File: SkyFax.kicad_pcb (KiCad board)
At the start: 2 copper layers, 60 parts, among them J1 RJ11/12, J2 DE9_Receptacle_MountingHoles, Q1 Q_NPN_BEC, Q2 Q_PNP_BEC, Q3 Q_NPN_BEC, Q4 Q_NPN_BEC, Q5 Q_NPN_BEC, Q6 Q_NPN_EBC, SW1 SW_DIP_x08, U1 Si2494-A-FM, U2 Si3018, U3 25LC640AT-E/SN, X1 ECS-2520MV-xxx-xx

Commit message: Sent to fab v1.0
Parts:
- removed kibuzzard-649E5FCF: G***, kibuzzard-649E5FCF
- removed kibuzzard-649E606C: G***, kibuzzard-649E606C
- removed kibuzzard-649E607D: G***, kibuzzard-649E607D
- removed kibuzzard-649E6159: G***, kibuzzard-649E6159
- added BZ1: Buzzer, Buzzer_Beeper:Buzzer_12x9.5RM7.6, F.Cu at (108.2, 146.6)
- added G***: LOGO, FaxCam:smiley_5.0x5.2mm, F.Cu at (151.1, 121.6)
- added J3: Conn_01x02, Connector_PinHeader_2.54mm:PinHeader_1x02_P2.54mm_Vertical, F.Cu at (95.8, 148.0)
- added kibuzzard-64A46BC3: G***, kibuzzard-64A46BC3, F.Cu at (161.6, 118.1)
- added kibuzzard-64A46BC7: G***, kibuzzard-64A46BC7, F.Cu at (152.9, 117.1)
- added kibuzzard-64A46BF2: G***, kibuzzard-64A46BF2, F.Cu at (156.7, 119.5)
- added kibuzzard-64A46C0A: G***, kibuzzard-64A46C0A, F.Cu at (160.1, 122.0)
- added kibuzzard-64A46CB2: G***, kibuzzard-64A46CB2, F.Cu at (97.0, 124.7)
- added kibuzzard-64A46CE2: G***, kibuzzard-64A46CE2, F.Cu at (99.6, 124.7)
- added kibuzzard-64A46CEC: G***, kibuzzard-64A46CEC, F.Cu at (102.1, 124.7)
- added kibuzzard-64A46CF4: G***, kibuzzard-64A46CF4, F.Cu at (104.6, 124.7)
- added kibuzzard-64A46CF9: G***, kibuzzard-64A46CF9, F.Cu at (107.2, 124.7)
- added kibuzzard-64A46D01: G***, kibuzzard-64A46D01, F.Cu at (109.7, 124.7)
- added kibuzzard-64A46D0F: G***, kibuzzard-64A46D0F, F.Cu at (112.3, 124.7)
- added kibuzzard-64A46D1C: G***, kibuzzard-64A46D1C, F.Cu at (114.8, 124.7)
- C3, C4, C5, C6, Q3, R1, R10, R11, R23, R3, R6, R9, U3, Z1: moved to F.Cu
- C50, C51, C52, R22: moved to B.Cu
- moved R14 77.7 mm to (97.3, 115.1), turned to -90 degrees
- moved R15 74.6 mm to (99.8, 115.1), turned to -90 degrees
- moved R16 71.5 mm to (102.4, 115.1), turned to -90 degrees
- moved R17 68.5 mm to (104.9, 115.1), turned to -90 degrees
- moved R18 65.5 mm to (107.4, 115.1), turned to -90 degrees
- moved SW1 64.9 mm to (106.2, 117.6), turned to 90 degrees
- moved J2 62.6 mm to (88.3, 139.4), turned to -90 degrees
- moved R19 62.6 mm to (110.0, 115.1), turned to -90 degrees
- moved R24 61.3 mm to (112.9, 134.2), turned to 180 degrees
- moved R41 60.6 mm to (111.5, 136.8), turned to 180 degrees
- moved R20 59.7 mm to (112.5, 115.1), turned to -90 degrees
- moved R21 57.0 mm to (115.1, 115.1), turned to -90 degrees
- moved C41 47.7 mm to (111.5, 138.6), turned to 180 degrees
- moved X1 47.5 mm to (99.9, 132.1), turned to 90 degrees
- moved R23 47.0 mm to (99.4, 141.0)
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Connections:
- SW1 pad 1: /nFSYNC -> /nINT
- SW1 pad 2: /nCTS -> /nFSYNC
- SW1 pad 3: /SDI -> /nDCD
- SW1 pad 4: /AOUT -> /SDI
- SW1 pad 5: /EECLK -> /nCTS
- SW1 pad 6: /nINT -> /EECLK
- SW1 pad 7: /nRI -> /AOUT
- SW1 pad 8: /nDCD -> /nRI
- U1 pad 39: (no net) -> GND
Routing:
- net +3V3: track 29.4 -> 72.4 mm, vias 3 -> 4
- net /nCTS: track 0.00 -> 41.1 mm, vias 0 -> 1
- net /nRI: track 14.0 -> 49.8 mm
- net /nDCD: track 0.00 -> 33.8 mm, vias 0 -> 1
- net /nRTS: track 0.00 -> 33.0 mm, vias 0 -> 1
- net /RXD: track 0.00 -> 31.6 mm, vias 0 -> 1
- net /TXD: track 0.00 -> 30.5 mm, vias 0 -> 1
- net /SDI: track 0.00 -> 19.0 mm, vias 0 -> 2
- net Net-(U2-RNG2): track 27.7 -> 8.78 mm
- net /nFSYNC: track 0.00 -> 16.7 mm, vias 0 -> 2
- net Net-(U2-DCT): track 21.0 -> 6.31 mm, vias 1 -> 0
- net /EECLK: track 15.1 -> 27.7 mm, vias 1 -> 3
- net /nINT: track 0.00 -> 12.3 mm
- net Net-(D1-Pad4): track 21.6 -> 10.7 mm
- net Net-(Q4-E): track 5.14 -> 15.7 mm, vias 0 -> 2
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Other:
- board outline added: 92.7 x 38.4 mm

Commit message: Layout v1.9 (not finished)
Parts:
- removed G***: LOGO, FaxCam:smiley_5.0x5.2mm
- removed SW1: SW_DIP_x08, Button_Switch_SMD:SW_DIP_SPSTx08_Slide_6.7x21.88mm_W6.73mm_P2.54mm_LowProfile_JPin
- removed kibuzzard-64A46BC3: G***, kibuzzard-64A46BC3
- removed kibuzzard-64A46BC7: G***, kibuzzard-64A46BC7
- removed kibuzzard-64A46BF2: G***, kibuzzard-64A46BF2
- removed kibuzzard-64A46C0A: G***, kibuzzard-64A46C0A
- removed kibuzzard-64A46CB2: G***, kibuzzard-64A46CB2
- removed kibuzzard-64A46CE2: G***, kibuzzard-64A46CE2
- removed kibuzzard-64A46CEC: G***, kibuzzard-64A46CEC
- removed kibuzzard-64A46CF4: G***, kibuzzard-64A46CF4
- removed kibuzzard-64A46CF9: G***, kibuzzard-64A46CF9
- removed kibuzzard-64A46D01: G***, kibuzzard-64A46D01
- removed kibuzzard-64A46D0F: G***, kibuzzard-64A46D0F
- removed kibuzzard-64A46D1C: G***, kibuzzard-64A46D1C
- added C11: 0.1uF, Capacitor_SMD:C_0603_1608Metric, F.Cu at (105.4, 157.2)
- added C12: 0.1uF, Capacitor_SMD:C_0603_1608Metric, B.Cu at (77.0, 146.3)
- added C13: 4.7uF, Capacitor_SMD:C_0402_1005Metric, B.Cu at (75.7, 146.3)
- added C16: 4.7uF, Capacitor_SMD:C_0402_1005Metric, F.Cu at (79.5, 144.0)
- added C17: 0.1uF, Capacitor_SMD:C_0603_1608Metric, F.Cu at (80.8, 144.0)
- added D2: LED, LED_SMD:LED_0201_0603Metric, F.Cu at (79.8, 155.0)
- added D3: LED, LED_SMD:LED_0201_0603Metric, F.Cu at (80.5, 155.0)
- added FB3: FerriteBead_Small, Inductor_SMD:L_0805_2012Metric, F.Cu at (93.7, 123.5)
- added FB4: FerriteBead_Small, Inductor_SMD:L_0805_2012Metric, F.Cu at (93.7, 126.2)
- added J4: Conn_02x02_Odd_Even, Connector_PinHeader_2.54mm:PinHeader_2x02_P2.54mm_Vertical, F.Cu at (107.7, 151.1)
- added JP1: Jumper_2_Open, Connector_PinHeader_2.54mm:PinHeader_1x02_P2.54mm_Vertical, F.Cu at (106.4, 141.5)
- added SW2: SW_Push, Button_Switch_SMD:SW_Tactile_SPST_NO_Straight_CK_PTS636Sx25SMTRLFS, F.Cu at (94.2, 140.2)
- added U4: CP2102N-Axx-xQFN20, Package_DFN_QFN:SiliconLabs_QFN-20-1EP_3x3mm_P0.5mm_EP1.8x1.8mm, B.Cu at (81.0, 150.9)
- added kibuzzard-64B47980: G***, kibuzzard-64B47980, F.Cu at (94.0, 151.6)
- added kibuzzard-64B4798B: G***, kibuzzard-64B4798B, F.Cu at (94.0, 149.1)
- added kibuzzard-64B47998: G***, kibuzzard-64B47998, F.Cu at (94.0, 144.0)
- added kibuzzard-64B479A1: G***, kibuzzard-64B479A1, F.Cu at (94.0, 146.6)
- added kibuzzard-64B479A8: G***, kibuzzard-64B479A8, F.Cu at (94.0, 154.2)
- added kibuzzard-64B479C8: G***, kibuzzard-64B479C8, F.Cu at (94.0, 157.0)
- C10, C8, C9, FB1, FB2, R15, R16, R22, R4, R7, R8: moved to F.Cu
- J2: value DE9_Receptacle_MountingHoles -> USB_B_Micro; footprint Connector_Dsub:DSUB-9_Female_Horizontal_P2.77x2.84mm_EdgePinOffset9.90mm_Housed_MountingHolesOffset11.32mm -> Connector_USB:USB_Micro-B_Amphenol_10118193-0001LF_Horizontal
- J3: value Conn_01x02 -> Conn_02x06_Odd_Even; footprint Connector_PinHeader_2.54mm:PinHeader_1x02_P2.54mm_Vertical -> Connector_PinHeader_2.54mm:PinHeader_2x06_P2.54mm_Vertical
- R17: value 10k -> 1k; footprint Resistor_SMD:R_0603_1608Metric -> Resistor_SMD:R_0402_1005Metric
- R18, R19: value 10k -> 220; footprint Resistor_SMD:R_0603_1608Metric -> Resistor_SMD:R_0402_1005Metric; moved to F.Cu
- R20: value 10k -> 22.1k; footprint Resistor_SMD:R_0603_1608Metric -> Resistor_SMD:R_0402_1005Metric
- R21: value 10k -> 47.5k; footprint Resistor_SMD:R_0603_1608Metric -> Resistor_SMD:R_0402_1005Metric; moved to F.Cu
- U3: moved to B.Cu
- moved J1 83.1 mm to (91.1, 84.3), turned to 0 degrees
- moved R7 58.7 mm to (125.5, 84.5), turned to 0 degrees
- moved FB1 57.7 mm to (93.7, 118.0)
- moved FB2 56.1 mm to (93.7, 120.7)
- moved Q5 54.7 mm to (89.0, 122.1), turned to 0 degrees
- moved R19 53.0 mm to (78.2, 157.5), turned to 0 degrees
- moved Q3 52.6 mm to (89.0, 113.2), turned to 0 degrees
- moved Q4 50.9 mm to (89.0, 117.7)
- moved R18 50.7 mm to (78.2, 156.5), turned to 0 degrees
- moved R8 50.1 mm to (125.5, 89.4)
- moved Q2 50.1 mm to (89.0, 108.8), turned to 0 degrees
- moved Q1 49.3 mm to (89.0, 104.3), turned to 0 degrees
- moved C8 46.5 mm to (105.5, 123.0), turned to 0 degrees
- moved R21 45.6 mm to (82.0, 146.6), turned to 90 degrees
- moved C6 45.6 mm to (104.0, 99.3), turned to 0 degrees
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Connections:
- net Net-(U1-C1A) renamed /C1A
- net Net-(U1-C2A) renamed /C2A
- net Net-(U1-CLKIN_XTAL1) renamed /CLK
- C8 pad 1: /RING -> Net-(C8-Pad1)
- C9 pad 1: /TIP -> Net-(C9-Pad1)
- FB1 pad 2: /RING -> Net-(C8-Pad1)
- FB2 pad 2: /TIP -> Net-(C9-Pad1)
- J2 pad 1: /nDCD -> VBUS
- J2 pad 2: /RXD -> /USB_DM
- J2 pad 3: /TXD -> /USB_DP
- J2 pad 6: unconnected-(J2-Pad6) -> GND
- J3 pad 1: +3V3 -> Net-(J3-Pin_1)
- J3 pad 2: GND -> /nCTS
- R14 pad 1: Net-(R14-Pad1) -> /nDCD
- R17 pad 1: Net-(R17-Pad1) -> VBUS
- R17 pad 2: GND -> Net-(U4-~{RST})
- R18 pad 1: Net-(R18-Pad1) -> +3V3
- R18 pad 2: GND -> Net-(D2-A)
- R19 pad 1: Net-(R19-Pad1) -> +3V3
- R19 pad 2: GND -> Net-(D3-A)
- R20 pad 1: Net-(R20-Pad1) -> VBUS
- R20 pad 2: GND -> Net-(U4-VBUS)
- R21 pad 1: Net-(R21-Pad1) -> Net-(U4-VBUS)
- R41 pad 2: /AOUT -> Net-(JP1-B)
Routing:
- net +3V3: track 72.4 -> 114.0 mm, vias 4 -> 7
- net /nRI: track 49.8 -> 16.3 mm
- net Net-(D1-+): track 28.5 -> 0.00 mm, vias 2 -> 0
- net /nCTS: track 41.1 -> 14.0 mm, vias 1 -> 0
- net /EECLK: track 27.7 -> 3.04 mm, vias 3 -> 1
- net Net-(Q1-E): track 24.1 -> 0.00 mm
- net Net-(Q4-B): track 22.4 -> 0.00 mm, vias 2 -> 0
- net Net-(Q1-B): track 22.4 -> 0.00 mm, vias 1 -> 0
- net /RXD: track 31.6 -> 9.86 mm, vias 1 -> 0
- net /nRTS: track 33.0 -> 11.7 mm
- net /nDCD: track 33.8 -> 13.2 mm, vias 1 -> 0
- net Net-(Q3-E): track 20.5 -> 0.00 mm, vias 2 -> 0
- net /TXD: track 30.5 -> 10.3 mm, vias 1 -> 0
- net Net-(U2-RNG1): track 17.8 -> 0.00 mm, vias 1 -> 0
- net Net-(Q3-B): track 17.6 -> 0.00 mm
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- removed copper zone on B.Cu, net GND1
- removed copper zone on F.Cu, net GND1
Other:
- board outline removed

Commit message: Sent to fab v2.0
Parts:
- added RV1: ~, Diode_SMD:D_SMB, F.Cu at (102.1, 79.4)
- added kibuzzard-64DEBF09: G***, kibuzzard-64DEBF09, F.Cu at (85.3, 100.3)
- added kibuzzard-64DEBF1B: G***, kibuzzard-64DEBF1B, F.Cu at (86.0, 92.5)
- added kibuzzard-64DEBF34: G***, kibuzzard-64DEBF34, F.Cu at (87.5, 97.7)
- moved R12 51.9 mm to (100.3, 138.9), turned to 90 degrees
- moved FB4 50.6 mm to (99.7, 75.9)
- moved C9 50.0 mm to (92.7, 79.6), turned to 180 degrees
- moved FB3 48.8 mm to (104.5, 75.9), turned to 180 degrees
- moved R10 48.4 mm to (87.1, 108.9), turned to 90 degrees
- moved R13 48.0 mm to (102.9, 138.9), turned to 90 degrees
- moved R9 44.1 mm to (93.3, 123.3), turned to -90 degrees
- moved C8 43.8 mm to (111.4, 79.6)
- moved R7 43.5 mm to (110.5, 125.3), turned to 180 degrees
- moved FB2 41.0 mm to (97.0, 79.9), turned to 90 degrees
- moved FB1 40.4 mm to (107.1, 79.9), turned to 90 degrees
- moved R6 40.2 mm to (96.1, 105.0)
- moved R8 35.3 mm to (110.5, 121.3)
- moved R5 33.3 mm to (105.5, 103.5)
- moved R1 32.1 mm to (87.8, 126.4), turned to 180 degrees
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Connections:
- net /C1A renamed /C1_P
- net /C2A renamed /C1_N
- net Net-(C1-Pad2) renamed /1_P
- net Net-(C2-Pad2) renamed /1_N
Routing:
- net GND: track 11.7 -> 135.4 mm, vias 5 -> 14
- net GND1: track 0.00 -> 74.7 mm, vias 0 -> 2
- net Net-(D1-Pad3): track 0.00 -> 51.1 mm
- net Net-(D1-Pad4): track 0.00 -> 47.2 mm
- net Net-(Q1-E): track 0.00 -> 35.2 mm, vias 0 -> 2
- net Net-(Q1-B): track 0.00 -> 32.1 mm, vias 0 -> 2
- net Net-(Q3-B): track 0.00 -> 29.7 mm, vias 0 -> 2
- net Net-(D1-+): track 0.00 -> 27.6 mm
- net Net-(C4-Pad1): track 0.00 -> 22.4 mm
- net Net-(Q3-E): track 0.00 -> 20.2 mm, vias 0 -> 2
- net Net-(Q2-B): track 0.00 -> 16.7 mm
- net Net-(Q5-C): track 0.00 -> 15.2 mm, vias 0 -> 2
- net Net-(U2-RX): track 0.00 -> 12.3 mm
- net /TIP: track 0.00 -> 10.8 mm
- net Net-(Q4-B): track 0.00 -> 10.7 mm
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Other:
- board outline added: 50.9 x 101.5 mm
- board text added: "@im_eningeer"

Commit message: Sent to fab v3.0
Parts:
- removed BZ1: Buzzer, Buzzer_Beeper:Buzzer_12x9.5RM7.6
- removed C11, C12, C17, C41, C50, C52: 0.1uF, Capacitor_SMD:C_0603_1608Metric
- removed C13, C16: 4.7uF, Capacitor_SMD:C_0402_1005Metric
- removed C51: 0.22uF, Capacitor_SMD:C_0603_1608Metric
- removed FB3, FB4: FerriteBead_Small, Inductor_SMD:L_0805_2012Metric
- removed JP1: Jumper_2_Open, Connector_PinHeader_2.54mm:PinHeader_1x02_P2.54mm_Vertical
- removed Q6: Q_NPN_EBC, Package_TO_SOT_THT:TO-92
- removed R14, R22, R23, R24: 10k, Resistor_SMD:R_0603_1608Metric
- removed R17: 1k, Resistor_SMD:R_0402_1005Metric
- removed R18, R19: 220, Resistor_SMD:R_0402_1005Metric
- removed R20: 22.1k, Resistor_SMD:R_0402_1005Metric
- removed R21: 47.5k, Resistor_SMD:R_0402_1005Metric
- removed R41: 150, Resistor_SMD:R_0603_1608Metric
- removed SW2: SW_Push, Button_Switch_SMD:SW_Tactile_SPST_NO_Straight_CK_PTS636Sx25SMTRLFS
- removed kibuzzard-64B47980: G***, kibuzzard-64B47980
- removed kibuzzard-64B4798B: G***, kibuzzard-64B4798B
- removed kibuzzard-64B47998: G***, kibuzzard-64B47998
- removed kibuzzard-64B479A1: G***, kibuzzard-64B479A1
- removed kibuzzard-64B479A8: G***, kibuzzard-64B479A8
- removed kibuzzard-64B479C8: G***, kibuzzard-64B479C8
- removed kibuzzard-64DEBF34: G***, kibuzzard-64DEBF34
- added C101: 4.7uF, Capacitor_SMD:C_0402_1005Metric, F.Cu at (47.3, 137.8)
- added C102: 0.1uF, Capacitor_SMD:C_0603_1608Metric, F.Cu at (47.0, 136.4)
- added C103: 4.7uF, Capacitor_SMD:C_0402_1005Metric, F.Cu at (51.6, 132.6)
- added C104: 0.1uF, Capacitor_SMD:C_0603_1608Metric, F.Cu at (54.4, 134.1)
- added C201: 0.1uF, Capacitor_SMD:C_0603_1608Metric, F.Cu at (92.1, 128.8)
- added C202: 0.1uF, Capacitor_SMD:C_0603_1608Metric, F.Cu at (92.1, 127.1)
- added C203: 0.22uF, Capacitor_SMD:C_0603_1608Metric, F.Cu at (92.8, 121.4)
- added C204: 0.1uF, Capacitor_SMD:C_0603_1608Metric, F.Cu at (79.9, 129.2)
- added D4: LED, LED_SMD:LED_0805_2012Metric, F.Cu at (50.5, 118.2)
- added D5: LED, LED_SMD:LED_0805_2012Metric, F.Cu at (50.5, 116.2)
- added D6: LED, LED_SMD:LED_0805_2012Metric, F.Cu at (50.5, 114.2)
- added D7: LED, LED_SMD:LED_0805_2012Metric, F.Cu at (50.5, 112.1)
- added J5: Conn_01x02, Connector_PinSocket_2.54mm:PinSocket_1x02_P2.54mm_Vertical, F.Cu at (104.0, 113.4)
- added J6: Conn_01x02, Connector_PinSocket_2.54mm:PinSocket_1x02_P2.54mm_Vertical, F.Cu at (145.6, 122.8)
- added R101: 1k, Resistor_SMD:R_0402_1005Metric, F.Cu at (59.2, 134.7)
- added R102: 22.1k, Resistor_SMD:R_0402_1005Metric, F.Cu at (56.9, 139.1)
- added R103: 47.5k, Resistor_SMD:R_0402_1005Metric, F.Cu at (56.9, 136.8)
- added R104: 220, LED_SMD:LED_0603_1608Metric, F.Cu at (53.9, 122.3)
- added R105: 220, LED_SMD:LED_0603_1608Metric, F.Cu at (54.0, 120.3)
- added R106: 220, LED_SMD:LED_0603_1608Metric, F.Cu at (54.0, 118.2)
- added R107: 220, LED_SMD:LED_0603_1608Metric, F.Cu at (54.0, 116.2)
- added R108: 220, LED_SMD:LED_0603_1608Metric, F.Cu at (54.0, 114.2)
- added R109: 220, LED_SMD:LED_0603_1608Metric, F.Cu at (54.0, 112.1)
- added R201: 10k, Resistor_SMD:R_0603_1608Metric, B.Cu at (83.2, 115.2)
- added R202: 10k, Resistor_SMD:R_0603_1608Metric, F.Cu at (82.2, 116.0)
- added R203: 10k, Resistor_SMD:R_0603_1608Metric, F.Cu at (91.9, 133.7)
- added R204: 10k, Resistor_SMD:R_0603_1608Metric, F.Cu at (91.9, 136.3)
- added R205: 10k, Resistor_SMD:R_0603_1608Metric, F.Cu at (80.7, 134.6)
- added R206: 10k, Resistor_SMD:R_0603_1608Metric, F.Cu at (80.7, 136.4)
- added SW1: SW_Push, Button_Switch_SMD:SW_Tactile_SPST_NO_Straight_CK_PTS636Sx25SMTRLFS, F.Cu at (88.4, 110.0)
- added U5: AZ1117-3.3, Package_TO_SOT_SMD:SOT-223-3_TabPin2, F.Cu at (52.3, 139.7)
- added U6: 74LCX541, Package_SO:SOIC-20W_7.5x12.8mm_P1.27mm, F.Cu at (63.8, 119.1)
- added U7: DS1818, Package_TO_SOT_SMD:SOT-23-3, F.Cu at (81.1, 111.3)
- added kibuzzard-64F3F98C: G***, kibuzzard-64F3F98C, F.Cu at (68.5, 139.8)
- added kibuzzard-64F3FC0B: G***, kibuzzard-64F3FC0B, F.Cu at (46.9, 122.3)
- added kibuzzard-64F3FC33: G***, kibuzzard-64F3FC33, F.Cu at (46.9, 120.3)
- added kibuzzard-64F3FC43: G***, kibuzzard-64F3FC43, F.Cu at (46.9, 118.2)
- added kibuzzard-64F3FC6A: G***, kibuzzard-64F3FC6A, F.Cu at (46.9, 116.2)
- added kibuzzard-64F3FC7E: G***, kibuzzard-64F3FC7E, F.Cu at (46.9, 114.2)
- added kibuzzard-64F3FC8A: G***, kibuzzard-64F3FC8A, F.Cu at (46.9, 112.1)
- C1, C2, C8, C9: footprint Capacitor_SMD:C_1812_4532Metric -> FaxCam:C_1808
- C4: footprint Capacitor_SMD:C_1206_3216Metric -> Capacitor_SMD:CP_Elec_4x3
- D1: value DF04S -> HDS10M; footprint Diode_SMD:Diode_Bridge_OnSemi_SDIP-4L -> FaxCam:Diodes_Inc_4-SMD
- D2, D3: footprint LED_SMD:LED_0201_0603Metric -> LED_SMD:LED_0805_2012Metric
- J2: value USB_B_Micro -> Conn_02x02_Odd_Even; footprint Connector_USB:USB_Micro-B_Amphenol_10118193-0001LF_Horizontal -> Connector_PinHeader_2.54mm:PinHeader_2x02_P2.54mm_Vertical
- J3: value Conn_02x06_Odd_Even -> USB_B_Micro; footprint Connector_PinHeader_2.54mm:PinHeader_2x06_P2.54mm_Vertical -> Connector_USB:USB_Micro-B_Amphenol_10118193-0001LF_Horizontal
- J4: value Conn_02x02_Odd_Even -> Conn_02x08_Odd_Even; footprint Connector_PinHeader_2.54mm:PinHeader_2x02_P2.54mm_Vertical -> Connector_PinSocket_2.54mm:PinSocket_2x08_P2.54mm_Vertical
- Q1, Q2, Q3, Q4, Q5: footprint Package_TO_SOT_SMD:SOT-23 -> Package_TO_SOT_SMD:SOT-23-3
- R1, R10, R11, R3, Z1: moved to B.Cu
- R15, R16: value 10k -> 0
- R4: footprint Resistor_SMD:R_1206_3216Metric -> Resistor_SMD:R_2010_5025Metric; moved to B.Cu
- R5: footprint Resistor_SMD:R_1210_3225Metric -> Resistor_SMD:R_0603_1608Metric
- R6: footprint Resistor_SMD:R_1210_3225Metric -> Resistor_SMD:R_0603_1608Metric; moved to B.Cu
- R7, R8: footprint Resistor_SMD:R_2512_6332Metric -> Resistor_SMD:R_0805_2012Metric
- R9: footprint Resistor_SMD:R_1206_3216Metric -> Resistor_SMD:R_0603_1608Metric; moved to B.Cu
- U3: value 25LC640AT-E/SN -> CP2102N-Axx-xQFN20; footprint Package_SO:SOIC-8_3.9x4.9mm_P1.27mm -> Package_DFN_QFN:SiliconLabs_QFN-20-1EP_3x3mm_P0.5mm_EP1.8x1.8mm; moved to F.Cu
- U4: value CP2102N-Axx-xQFN20 -> 25LC640AT-E/SN; footprint Package_DFN_QFN:SiliconLabs_QFN-20-1EP_3x3mm_P0.5mm_EP1.8x1.8mm -> Package_SO:SOIC-8_3.9x4.9mm_P1.27mm
- moved J1 70.4 mm to (149.2, 126.7), turned to 90 degrees
- moved C9 68.6 mm to (138.2, 130.9), turned to -90 degrees
- moved RV1 56.6 mm to (138.6, 122.7), turned to 90 degrees
- moved C8 56.5 mm to (135.1, 130.9), turned to -90 degrees
- moved FB2 55.9 mm to (132.8, 122.8), turned to -90 degrees
- moved FB1 55.3 mm to (142.0, 122.8), turned to -90 degrees
- moved U3 51.2 mm to (58.2, 130.4), turned to 0 degrees
- moved Z1 48.8 mm to (140.2, 111.5), turned to 180 degrees
- moved Q2 47.5 mm to (140.8, 111.5), turned to 0 degrees
- moved kibuzzard-64DEBF1B 47.4 mm to (73.7, 138.2), turned to 0 degrees
- moved D1 46.4 mm to (139.2, 116.2)
- moved D3 45.9 mm to (50.5, 120.3), turned to 180 degrees
- moved D2 43.9 mm to (50.5, 122.3), turned to 180 degrees
- moved R16 43.6 mm to (141.9, 127.9), turned to -90 degrees
- moved J3 43.1 mm to (46.2, 129.8), turned to -90 degrees
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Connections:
- net /1_N renamed Net-(C2-Pad2)
- net /1_P renamed Net-(C1-Pad2)
- net /C1_N renamed /SI2494/C2A
- net /C1_P renamed /SI2494/C1A
- net /CLK renamed Net-(U1-CLKIN_XTAL1)
- net Net-(U2-C1B) renamed /SI3018/C1A
- net Net-(U2-C2B) renamed /SI3018/C2A
- D1 pad 2: GND1 -> Net-(D1-Pad2)
- D1 pad 3: Net-(D1-Pad3) -> GND1
- D2 pad 2: Net-(D2-A) -> +3V3
- D3 pad 2: Net-(D3-A) -> +3V3
- FB1 pad 1: Net-(D1-Pad3) -> Net-(D1-Pad4)
- FB1 pad 2: Net-(C8-Pad1) -> Net-(C9-Pad1)
- FB2 pad 1: Net-(D1-Pad4) -> Net-(D1-Pad2)
- FB2 pad 2: Net-(C9-Pad1) -> Net-(C8-Pad1)
- J1 pad 3: /RING -> /SI3018/TIP
- J1 pad 4: /TIP -> /SI3018/RING
- J2 pad 1: VBUS -> /SI2494/SDI
- J2 pad 2: /USB_DM -> Net-(J2-Pin_2)
- J2 pad 3: /USB_DP -> /SI2494/nFSYNC
- J2 pad 4: unconnected-(J2-ID-Pad4) -> Net-(J2-Pin_4)
- J3 pad 1: Net-(J3-Pin_1) -> VBUS
- J3 pad 2: /nCTS -> Net-(J3-D-)
- J3 pad 3: Net-(J3-Pin_3) -> Net-(J3-D+)
- J3 pad 4: /nRTS -> unconnected-(J3-ID-Pad4)
- J3 pad 5: Net-(J3-Pin_5) -> GND
- J3 pad 6: /RXD -> GND
- J4 pad 1: /SDI -> +3V3
- J4 pad 2: Net-(J4-Pin_2) -> +3V3
- J4 pad 3: /nFSYNC -> /USB_Serial/TXD
- J4 pad 4: Net-(J4-Pin_4) -> /SI2494/TXD
- Q3 pad 2: Net-(Q2-B) -> Net-(Q3-E)
- Q3 pad 3: Net-(Q3-E) -> Net-(Q2-B)
- R15 pad 1: Net-(J4-Pin_2) -> Net-(C8-Pad1)
- R15 pad 2: GND -> /SI3018/RING
- R16 pad 1: Net-(J4-Pin_4) -> Net-(C9-Pad1)
- R16 pad 2: GND -> /SI3018/TIP
- R7 pad 1: Net-(D1-Pad3) -> Net-(D1-Pad2)
- RV1 pad 1: /TIP -> /SI3018/TIP
- RV1 pad 2: /RING -> /SI3018/RING
- U1 pad 10: /EESDI -> /SI2494/EESDI
- U1 pad 11: /EESDO -> /SI2494/EESDO
- U1 pad 12: /EECS -> /SI2494/EECS
- U1 pad 13: /EECLK -> /SI2494/EECLK
- U1 pad 15: /AOUT -> unconnected-(U1-AOUT-Pad15)
- U1 pad 16: /RST -> /SI2494/RST
- U1 pad 19: /nRI -> /SI2494/nRI
- U1 pad 2: /nFSYNC -> /SI2494/nFSYNC
- U1 pad 21: /nCTS -> /SI2494/nCTS
- U1 pad 22: /RXD -> /SI2494/RXD
- U1 pad 23: /TXD -> /SI2494/TXD
- U1 pad 24: /nRTS -> /SI2494/nRTS
- U1 pad 28: /nDCD -> /SI2494/nDCD
- U1 pad 35: /nINT -> unconnected-(U1-nINT-Pad35)
- U1 pad 8: /SDI -> /SI2494/SDI
- U3 pad 1: /EECS -> /USB_Serial/DCD
- U3 pad 2: /EESDO -> /USB_Serial/RI
- U3 pad 3: Net-(U3-~{WP}) -> GND
- U3 pad 4: GND -> Net-(J3-D+)
- U3 pad 5: /EESDI -> Net-(J3-D-)
- U3 pad 6: /EECLK -> +3V3
- U3 pad 7: Net-(U3-~{HOLD}) -> +3V3
- U3 pad 8: +3V3 -> Net-(U3-VBUS)
- U4 pad 1: Net-(J3-Pin_9) -> /SI2494/EECS
- U4 pad 2: Net-(J3-Pin_11) -> /SI2494/EESDO
- U4 pad 3: GND -> Net-(U4-~{WP})
- U4 pad 4: /USB_DP -> GND
- U4 pad 5: /USB_DM -> /SI2494/EESDI
- U4 pad 6: +3V3 -> /SI2494/EECLK
- U4 pad 7: VBUS -> Net-(U4-~{HOLD})
- U4 pad 8: Net-(U4-VBUS) -> +3V3
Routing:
- net Net-(D1-Pad3): track 51.1 -> 0.00 mm
- net GND: track 135.4 -> 85.5 mm, vias 14 -> 22
- net +3V3: track 114.0 -> 156.3 mm
- net Net-(D1-Pad2): track 0.00 -> 36.8 mm, vias 0 -> 2
- net /USB_Serial/RI: track 0.00 -> 29.2 mm
- net /USB_Serial/DCD: track 0.00 -> 27.8 mm, vias 0 -> 2
- net /USB_Serial/CTS: track 0.00 -> 22.8 mm
- net /USB_Serial/RTS: track 0.00 -> 21.1 mm, vias 0 -> 2
- net /USB_Serial/TXD: track 0.00 -> 21.0 mm, vias 0 -> 2
- net /SI2494/EECLK: track 0.00 -> 20.9 mm, vias 0 -> 1
- net /SI2494/nFSYNC: track 0.00 -> 20.5 mm, vias 0 -> 1
- net /USB_Serial/RXD: track 0.00 -> 20.0 mm, vias 0 -> 2
- net /SI2494/SDI: track 0.00 -> 19.7 mm, vias 0 -> 1
- net Net-(U4-~{WP}): track 0.00 -> 19.6 mm, vias 0 -> 3
- net /SI3018/RING: track 0.00 -> 18.4 mm, vias 0 -> 2
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- added copper zone on B.Cu, net GND1
- added copper zone on B.Cu, net Net-(Q1-E)
- added copper zone on F.Cu, net Net-(Q1-E)
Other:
- board size 50.9 x 101.5 mm -> 122.3 x 37.6 mm
- board text added: "Intentionally left empty (DRC/ERC will fail here)"

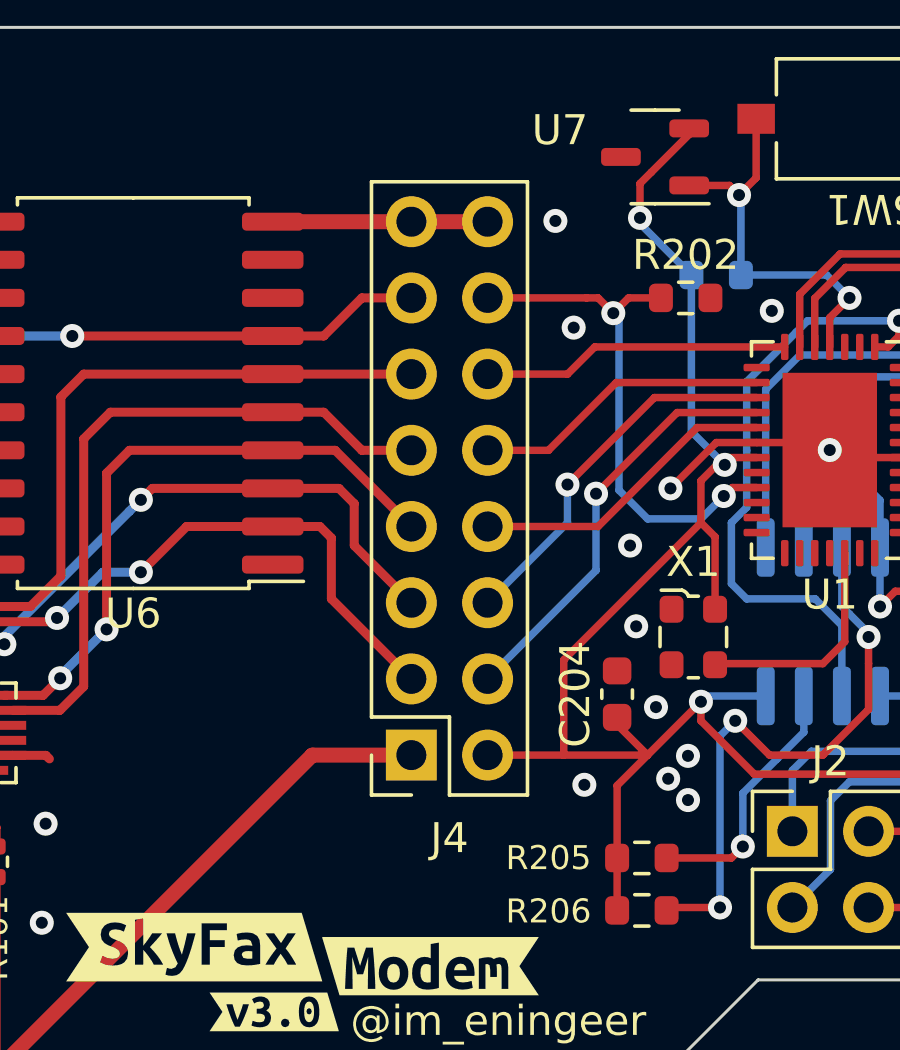
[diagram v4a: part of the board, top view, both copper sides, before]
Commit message: Version 3.0 minor BOM changes
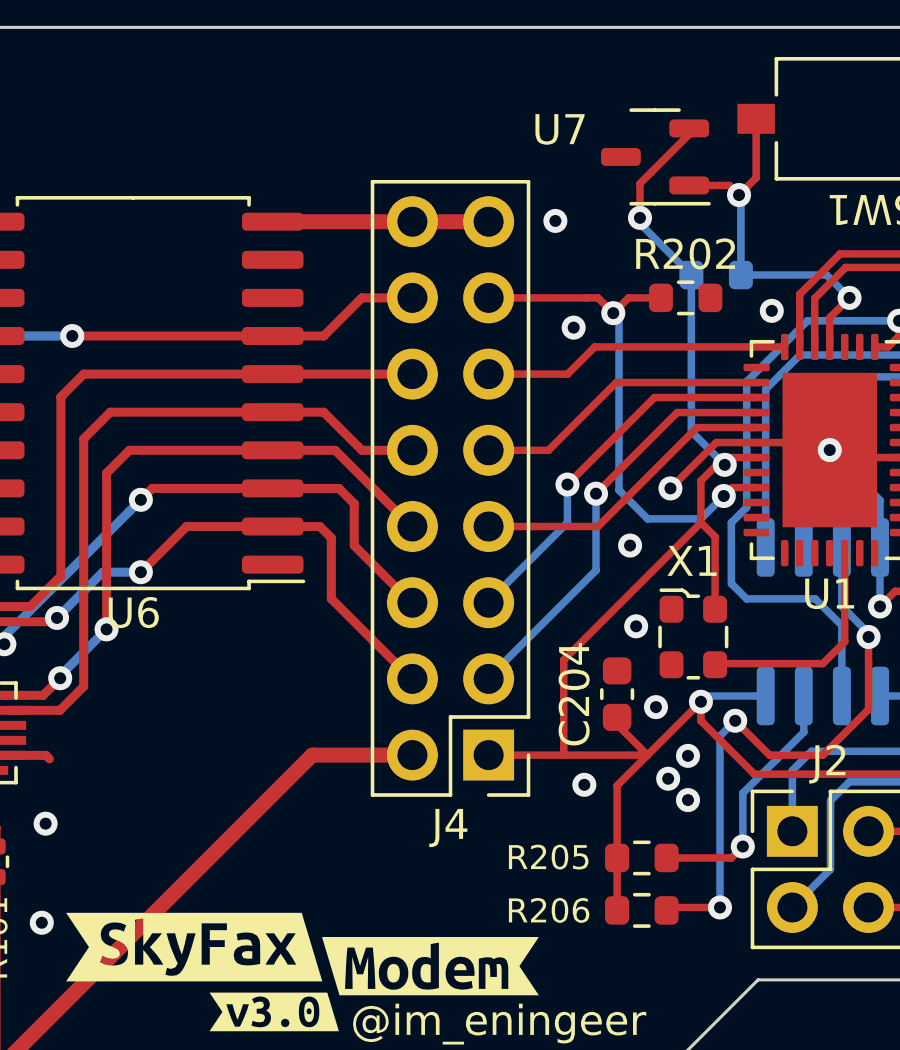
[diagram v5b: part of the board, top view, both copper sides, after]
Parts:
- J4: footprint Connector_PinSocket_2.54mm:PinSocket_2x08_P2.54mm_Vertical -> Connector_PinHeader_2.54mm:PinHeader_2x08_P2.54mm_Vertical
- moved J4 2.57 mm to (75.6, 131.2)

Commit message: Version 3.0 ERC/DRC fixes
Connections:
- J4 pad 10: /SI2494/nCTS -> /USB_Serial/CTS
- J4 pad 11: /USB_Serial/RI -> /SI2494/nRI
- J4 pad 12: /SI2494/nRI -> /USB_Serial/RI
- J4 pad 13: /USB_Serial/DCD -> /SI2494/nDCD
- J4 pad 14: /SI2494/nDCD -> /USB_Serial/DCD
- J4 pad 3: /USB_Serial/TXD -> /SI2494/TXD
- J4 pad 4: /SI2494/TXD -> /USB_Serial/TXD
- J4 pad 5: /USB_Serial/RXD -> /SI2494/RXD
- J4 pad 6: /SI2494/RXD -> /USB_Serial/RXD
- J4 pad 7: /USB_Serial/RTS -> /SI2494/nRTS
- J4 pad 8: /SI2494/nRTS -> /USB_Serial/RTS
- J4 pad 9: /USB_Serial/CTS -> /SI2494/nCTS
